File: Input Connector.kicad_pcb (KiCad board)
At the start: 2 copper layers, 81.8 x 33.5 mm, 3 parts, among them J1 776228-2, J2 RS-485/CAN, J3 V IN

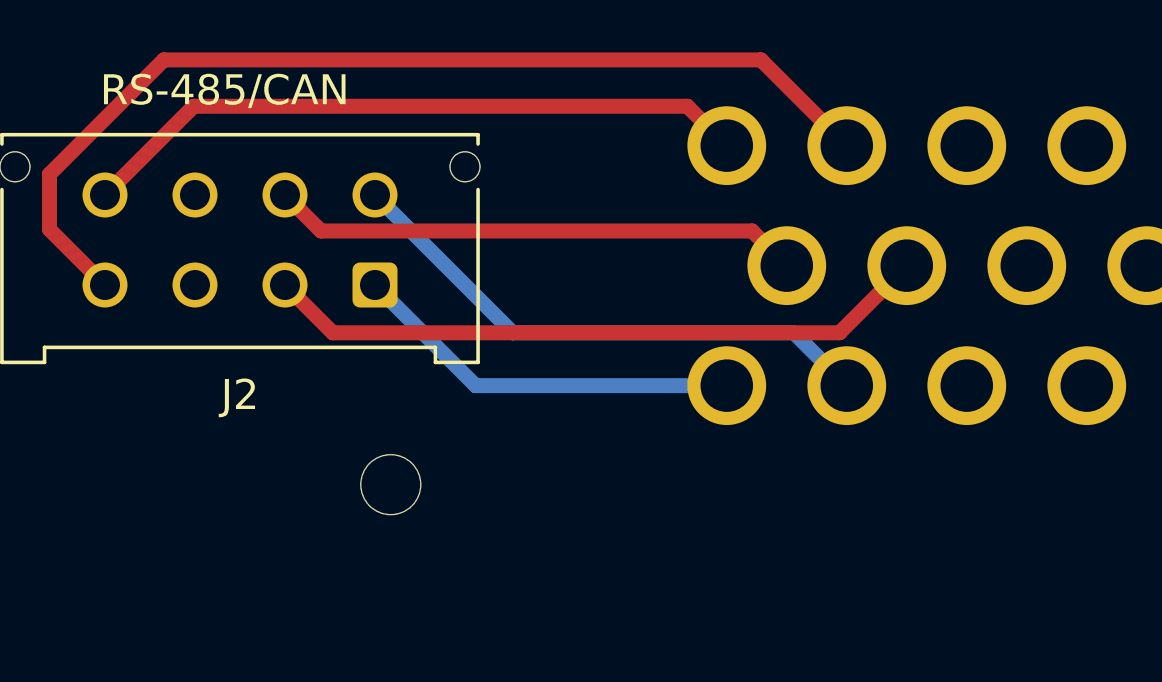
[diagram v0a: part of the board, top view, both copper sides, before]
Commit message: Добавил землю RS-484
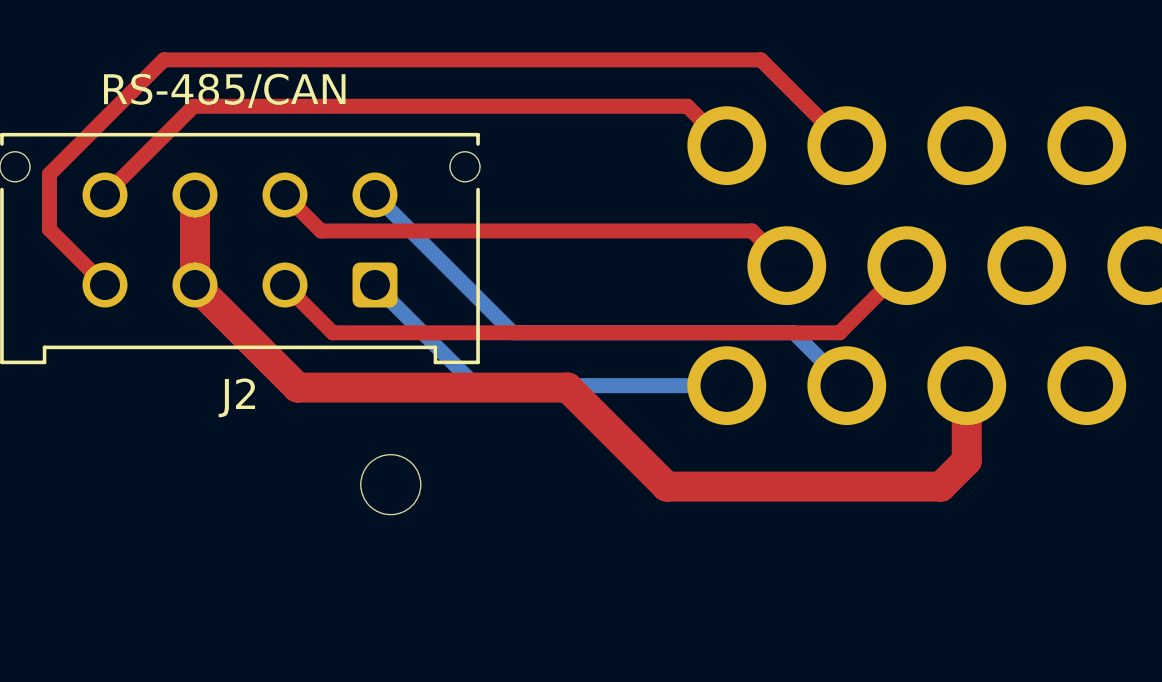
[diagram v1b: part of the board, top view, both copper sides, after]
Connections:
- J1 pad 21: unconnected-(J1-Pad21) -> GND
- J2 pad 3: GNDD -> GND
- J2 pad 7: VDD -> GND
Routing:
- net GND: track 0.00 -> 34.4 mm
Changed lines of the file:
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@@
   (net 19 "unconnected-(J1-Pad19)")
   (net 20 "unconnected-(J1-Pad20)")
-  (net 21 "unconnected-(J1-Pad21)")
-  (net 22 "/Y")
-  (net 23 "/Z")
+  (net 21 "/Y")
+  (net 22 "/Z")
+  (net 23 "GND")
   (footprint "Connector_Molex:Molex_Micro-Fit_3.0_43045-0412_2x02_P3.00mm_Vertical" (layer "F.Cu")
     (at 94.996 84.836 180)
@@
     (pad "" np_thru_hole circle (at 12 3.94 180) (size 1 1) (drill 1) (layers *.Cu *.Mask))
     (pad "1" thru_hole roundrect (at 0 0 180) (size 1.5 1.5) (drill 1) (layers *.Cu *.Mask) (roundrect_rratio 0.1666673333)
-      (net 23 "/Z") (pinfunction "Pin_1") (pintype "passive"))
+      (net 22 "/Z") (pinfunction "Pin_1") (pintype "passive"))
     (pad "2" thru_hole circle (at 3 0 180) (size 1.5 1.5) (drill 1) (layers *.Cu *.Mask)
       (net 14 "/A") (pinfunction "Pin_2") (pintype "passive"))
     (pad "3" thru_hole circle (at 6 0 180) (size 1.5 1.5) (drill 1) (layers *.Cu *.Mask)
-      (net 16 "GNDD") (pinfunction "Pin_3") (pintype "passive"))
+      (net 23 "GND") (pinfunction "Pin_3") (pintype "passive"))
     (pad "4" thru_hole circle (at 9 0 180) (size 1.5 1.5) (drill 1) (layers *.Cu *.Mask)
       (net 7 "/CANH") (pinfunction "Pin_4") (pintype "passive"))
     (pad "5" thru_hole circle (at 0 3 180) (size 1.5 1.5) (drill 1) (layers *.Cu *.Mask)
-      (net 22 "/Y") (pinfunction "Pin_5") (pintype "passive"))
+      (net 21 "/Y") (pinfunction "Pin_5") (pintype "passive"))
     (pad "6" thru_hole circle (at 3 3 180) (size 1.5 1.5) (drill 1) (layers *.Cu *.Mask)
       (net 15 "/B") (pinfunction "Pin_6") (pintype "passive"))
     (pad "7" thru_hole circle (at 6 3 180) (size 1.5 1.5) (drill 1) (layers *.Cu *.Mask)
-      (net 1 "VDD") (pinfunction "Pin_7") (pintype "passive"))
+      (net 23 "GND") (pinfunction "Pin_7") (pintype "passive"))
     (pad "8" thru_hole circle (at 9 3 180) (size 1.5 1.5) (drill 1) (layers *.Cu *.Mask)
       (net 8 "/CANL") (pinfunction "Pin_8") (pintype "passive"))
@@
       (net 20 "unconnected-(J1-Pad20)") (pinfunction "20") (pintype "passive"))
     (pad "21" thru_hole circle (at 6 -4 180) (size 2.625 2.625) (drill 1.75) (layers *.Cu *.Mask)
-      (net 21 "unconnected-(J1-Pad21)") (pinfunction "21") (pintype "passive"))
+      (net 23 "GND") (pinfunction "21") (pintype "passive"))
     (pad "22" thru_hole circle (at 10 -4 180) (size 2.625 2.625) (drill 1.75) (layers *.Cu *.Mask)
-      (net 22 "/Y") (pinfunction "22") (pintype "passive"))
+      (net 21 "/Y") (pinfunction "22") (pintype "passive"))
     (pad "23" thru_hole circle (at 14 -4 180) (size 2.625 2.625) (drill 1.75) (layers *.Cu *.Mask)
-      (net 23 "/Z") (pinfunction "23") (pintype "passive"))
+      (net 22 "/Z") (pinfunction "23") (pintype "passive"))
     (model "C:/Users/User/Desktop/Проекты/Модели 3D/776228-2.step"
       (offset (xyz 0 0 34))
@@
   (segment (start 125.922 84.074) (end 124.766511 82.918511) (width 0.5) (layer "F.Cu") (net 15))
   (segment (start 124.766511 82.918511) (end 110.395511 82.918511) (width 0.5) (layer "F.Cu") (net 15))
-  (segment (start 127.922 88.074) (end 126.159989 86.311989) (width 0.5) (layer "B.Cu") (net 22))
-  (segment (start 116.788989 86.311989) (end 112.196 81.719) (width 0.5) (layer "B.Cu") (net 22))
-  (segment (start 126.159989 86.311989) (end 116.788989 86.311989) (width 0.5) (layer "B.Cu") (net 22))
-  (segment (start 123.922 88.074) (end 115.551 88.074) (width 0.5) (layer "B.Cu") (net 23))
-  (segment (start 115.551 88.074) (end 112.196 84.719) (width 0.5) (layer "B.Cu") (net 23))
+  (segment (start 127.922 88.074) (end 126.159989 86.311989) (width 0.5) (layer "B.Cu") (net 21))
+  (segment (start 116.788989 86.311989) (end 112.196 81.719) (width 0.5) (layer "B.Cu") (net 21))
+  (segment (start 126.159989 86.311989) (end 116.788989 86.311989) (width 0.5) (layer "B.Cu") (net 21))
+  (segment (start 123.922 88.074) (end 115.551 88.074) (width 0.5) (layer "B.Cu") (net 22))
+  (segment (start 115.551 88.074) (end 112.196 84.719) (width 0.5) (layer "B.Cu") (net 22))
+  (segment (start 131.064 91.44) (end 131.922 90.582) (width 1) (layer "F.Cu") (net 23))
+  (segment (start 131.922 90.582) (end 131.922 88.074) (width 1) (layer "F.Cu") (net 23))
+  (segment (start 121.92 91.44) (end 131.064 91.44) (width 1) (layer "F.Cu") (net 23))
+  (segment (start 109.615 88.138) (end 118.618 88.138) (width 1) (layer "F.Cu") (net 23))
+  (segment (start 118.618 88.138) (end 121.92 91.44) (width 1) (layer "F.Cu") (net 23))
+  (segment (start 106.196 81.719) (end 106.196 84.719) (width 1) (layer "F.Cu") (net 23))
+  (segment (start 106.196 84.719) (end 109.615 88.138) (width 1) (layer "F.Cu") (net 23))
   (zone (net 16) (net_name "GNDD") (layer "F.Cu") (hatch edge 0.508)
     (connect_pads yes (clearance 1))
